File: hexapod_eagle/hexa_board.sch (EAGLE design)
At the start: 53 parts

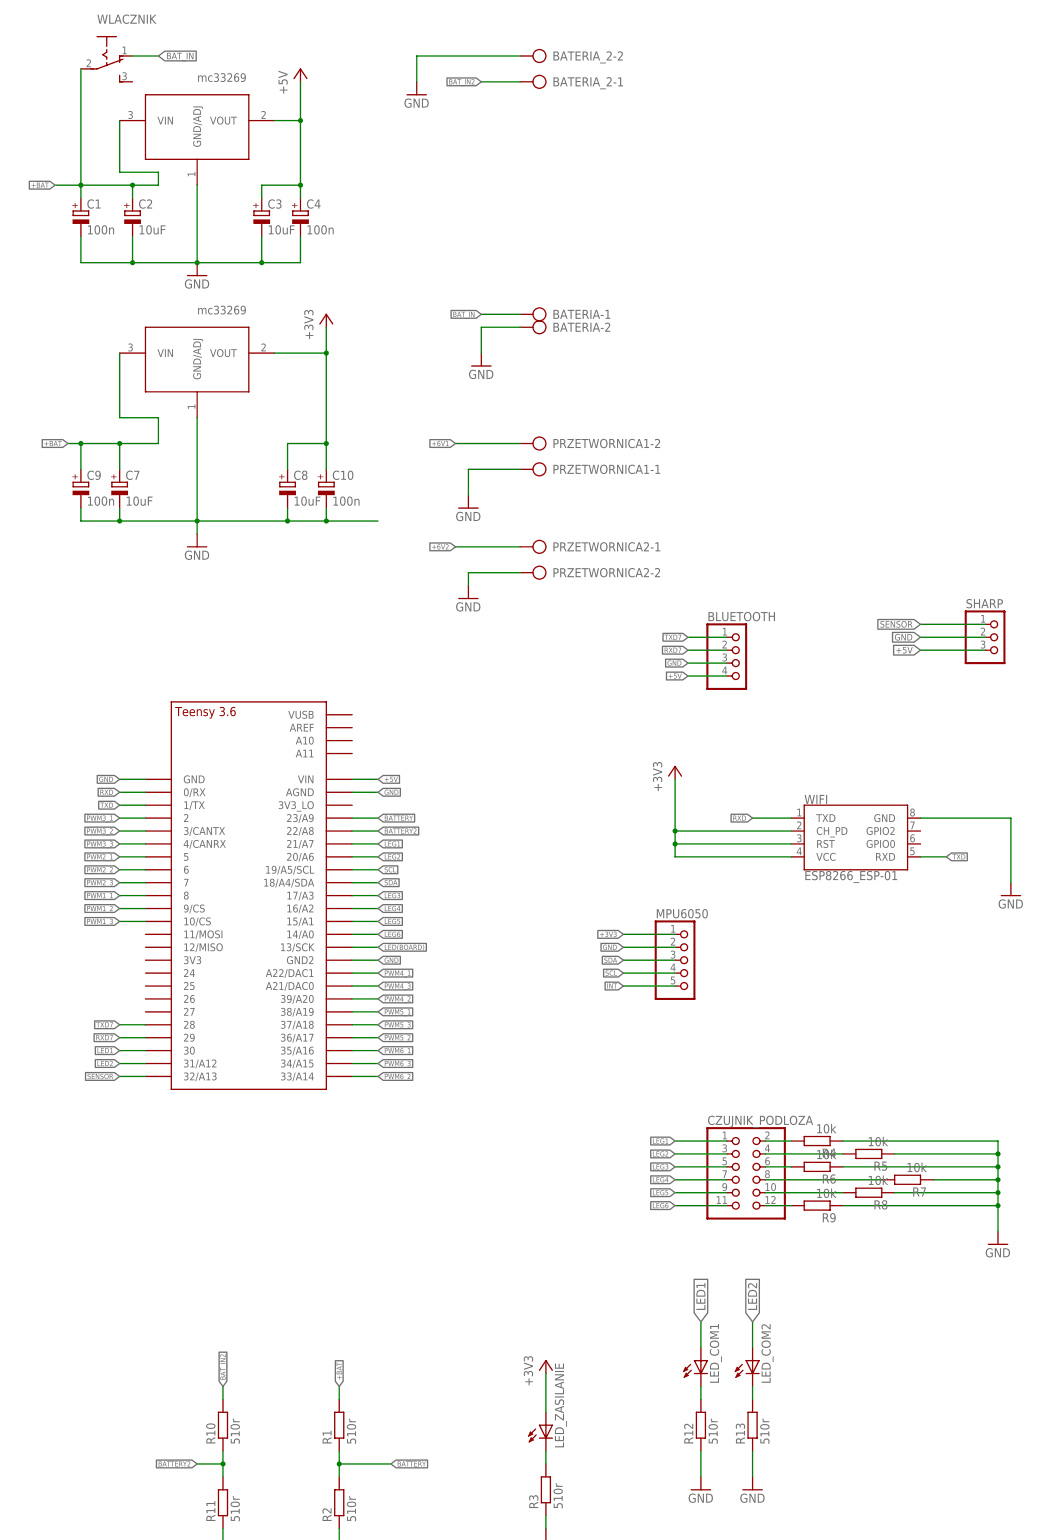
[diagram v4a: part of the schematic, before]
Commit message: Update eagle files
-change to ark leg sensor pins
-change isolte value
-esp32 cam-insted bluetooth/"wifi"
-some minor changes
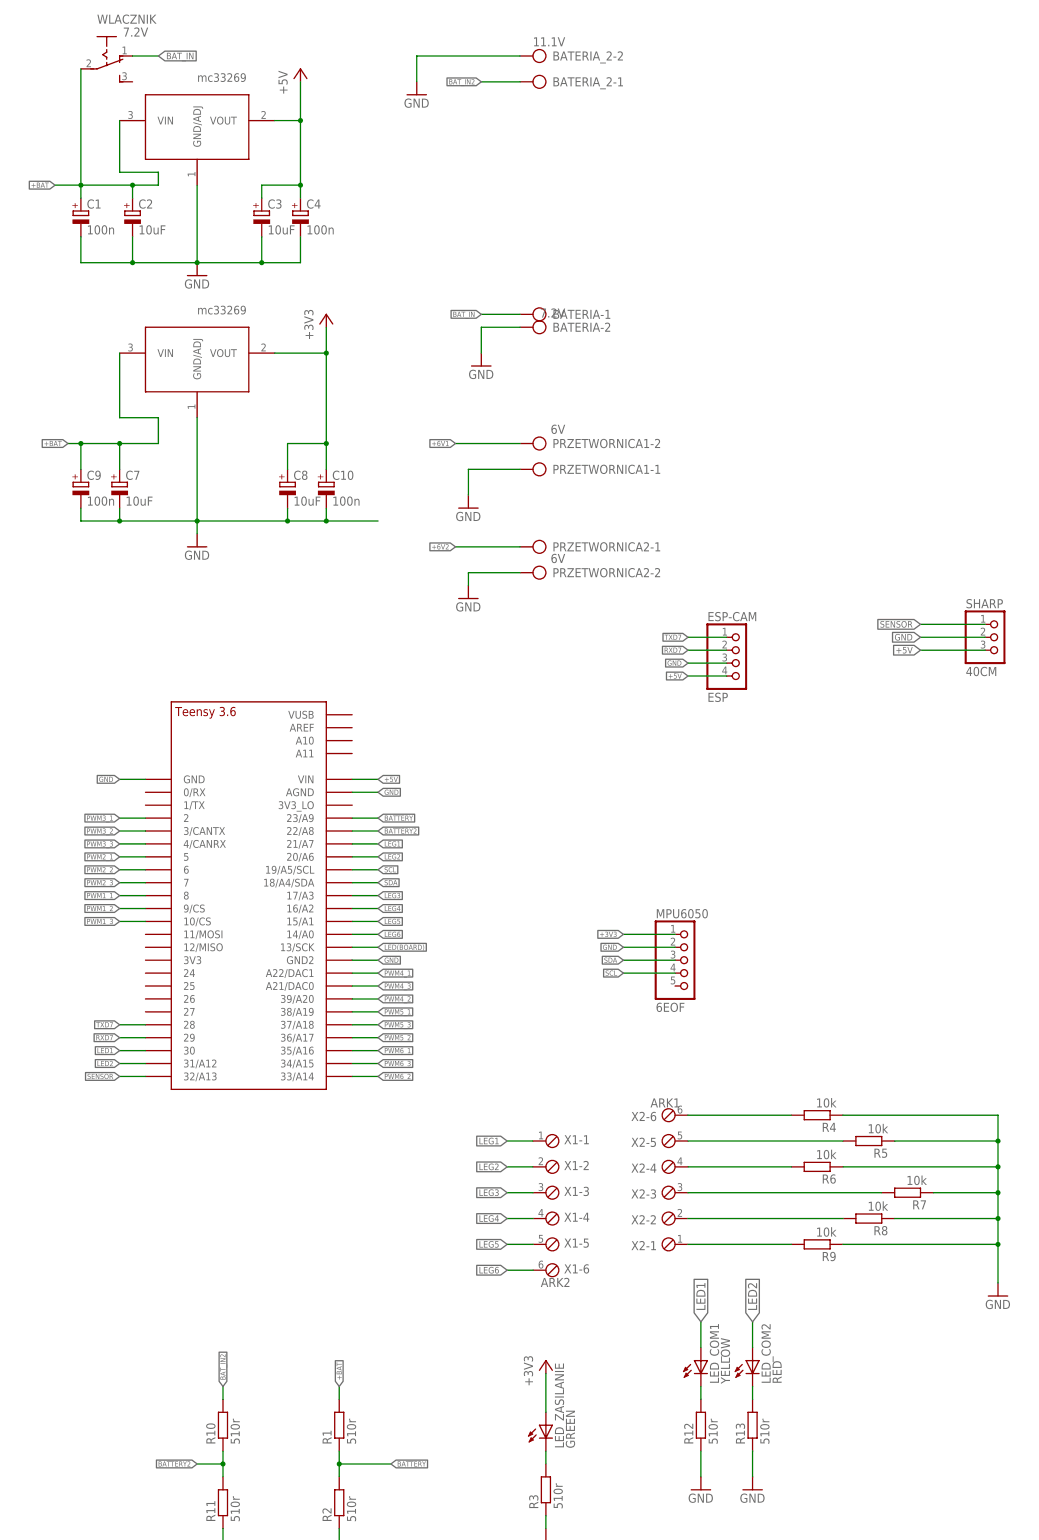
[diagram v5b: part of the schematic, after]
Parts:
- removed CZUJNIK_PODLOZA: (no value), pinhead:PINHD-2X6
- removed WIFI: ESP8266_ESP-01, SparkFun-RF:ESP8266_ESP-01
- added X1: ARK2, con-phoenix-254:MPT6
- added X2: ARK1, con-phoenix-254:MPT6
- BATERIA, WLACZNIK: value (none) -> 7.2V
- BATERIA_2: value (none) -> 11.1V
- ESP-CAM: value (none) -> ESP
- LED_COM1: value (none) -> YELLOW
- LED_COM2: value (none) -> RED
- LED_ZASILANIE: value (none) -> GREEN
- MPU6050: value (none) -> 6EOF
- PRZETWORNICA1, PRZETWORNICA2: value (none) -> 6V
- SHARP: value (none) -> 40CM
- renumbered BLUETOOTH to ESP-CAM
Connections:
- removed net INT: MPU6050.5
- removed net RXD: TEENSY41.0/RX, WIFI.TXD
- removed net TXD: TEENSY41.1/TX, WIFI.RXD
- net +3V3: no longer WIFI.CH_PD, WIFI.RST, WIFI.VCC
- net GND: no longer WIFI.GND
- net LEG1: now also X1-1.1; no longer CZUJNIK_PODLOZA.1
- net LEG2: now also X1-2.1; no longer CZUJNIK_PODLOZA.3
- net LEG3: now also X1-3.1; no longer CZUJNIK_PODLOZA.5
- net LEG4: now also X1-4.1; no longer CZUJNIK_PODLOZA.7
- net LEG5: now also X1-5.1; no longer CZUJNIK_PODLOZA.9
- net LEG6: now also X1-6.1; no longer CZUJNIK_PODLOZA.11
- net N$1: now also X2-6.1; no longer CZUJNIK_PODLOZA.2
- net N$2: now also X2-5.1; no longer CZUJNIK_PODLOZA.4
- net N$3: now also X2-4.1; no longer CZUJNIK_PODLOZA.6
- net N$5: now also X2-3.1; no longer CZUJNIK_PODLOZA.8
- net N$6: now also X2-2.1; no longer CZUJNIK_PODLOZA.10
- net N$7: now also X2-1.1; no longer CZUJNIK_PODLOZA.12
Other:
- moved on the sheet: R4, R5, R7, R8, R9

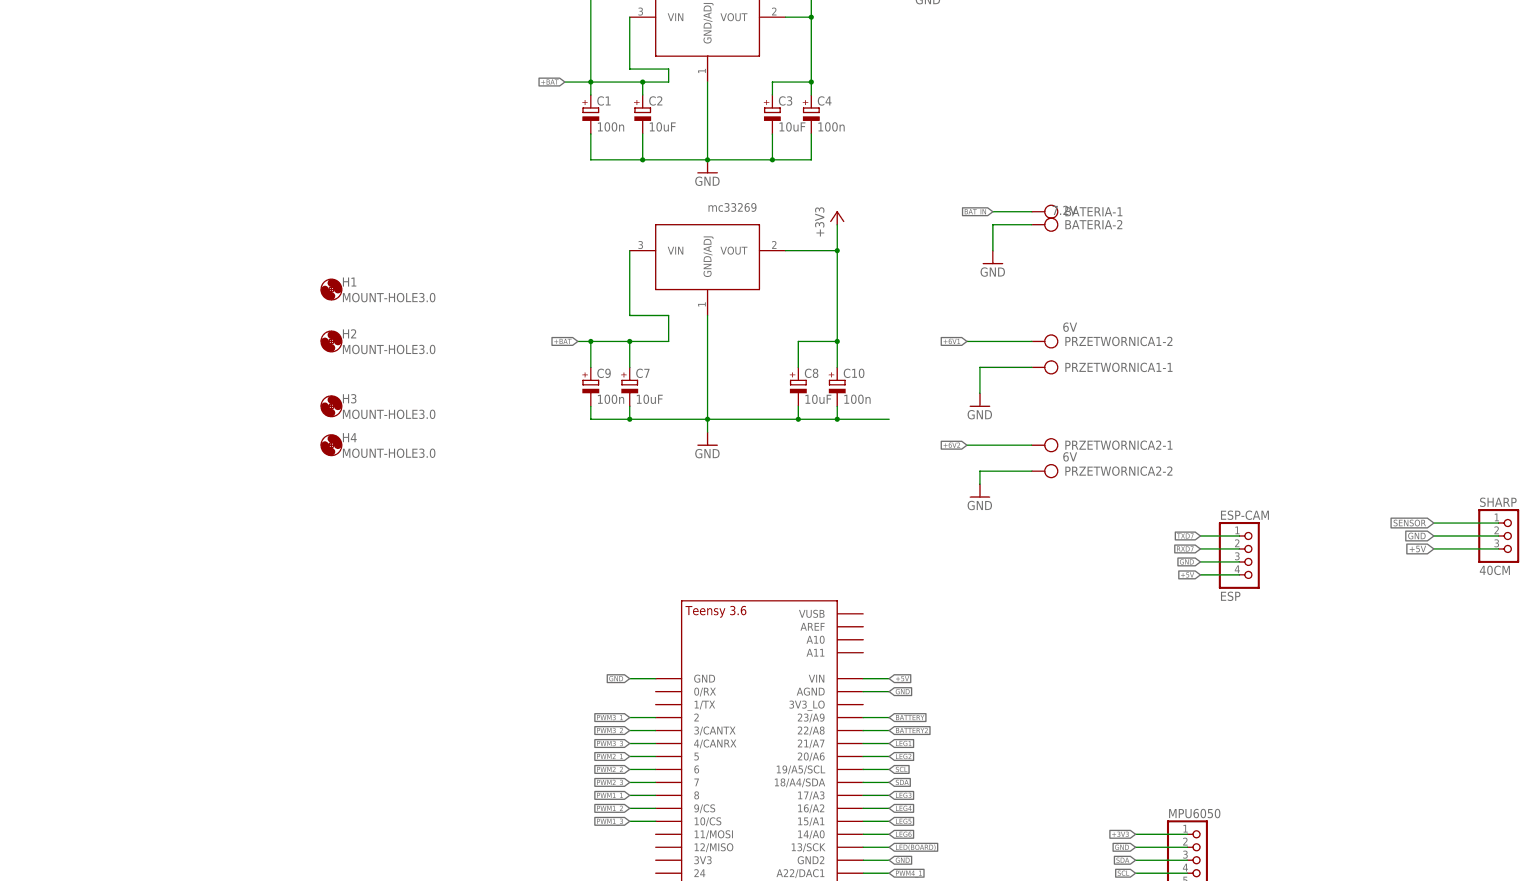
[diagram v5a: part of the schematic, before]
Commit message: Update eagle schematic and board
-added capacitors
-added voltage divider
-change package some capacitors
-added on/off swich for power mcu
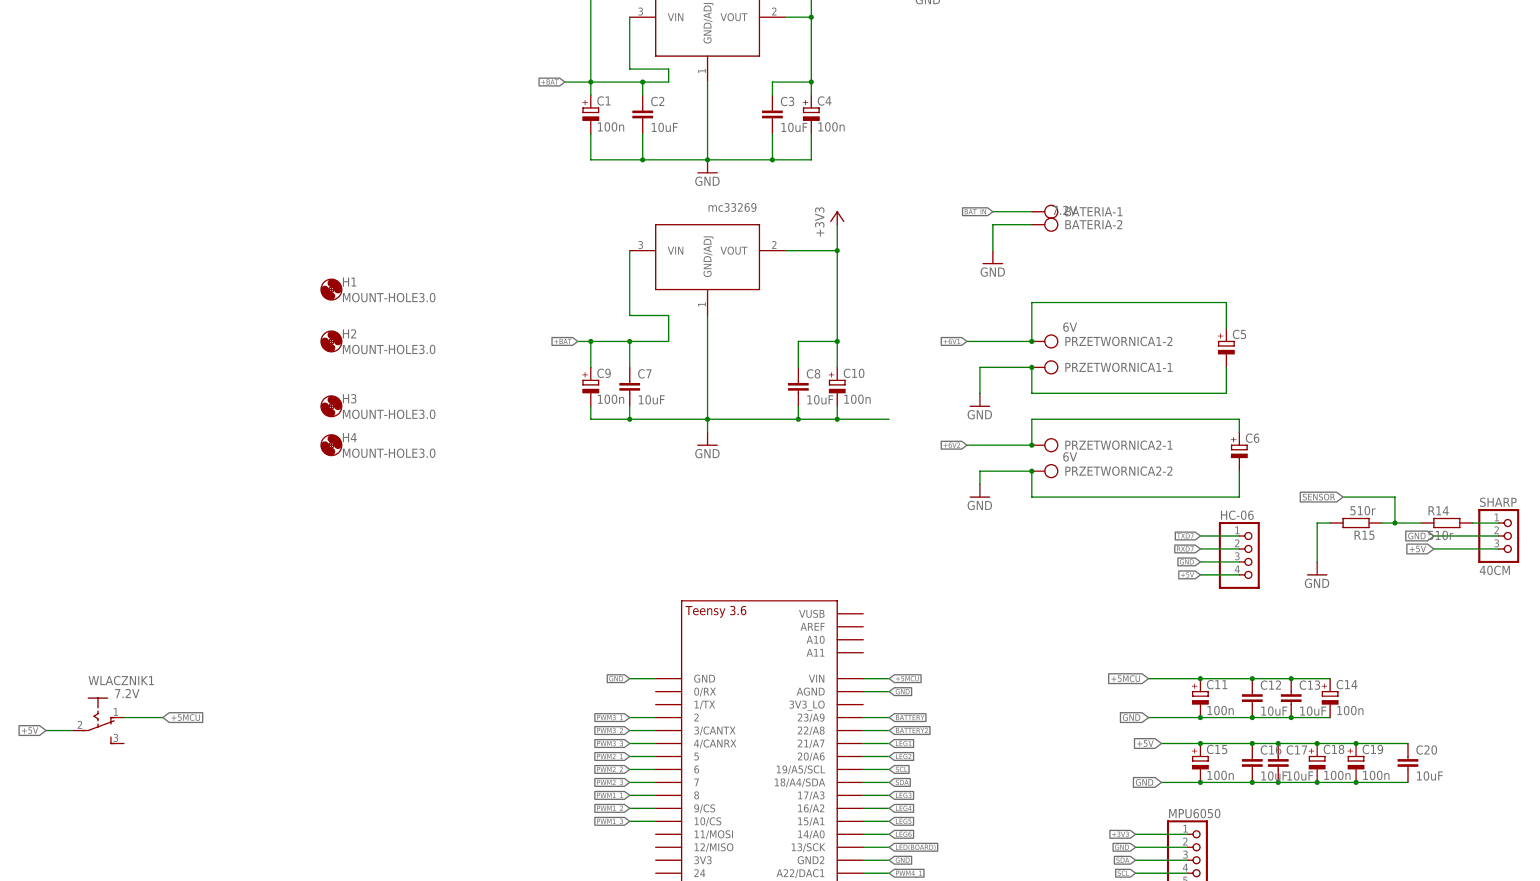
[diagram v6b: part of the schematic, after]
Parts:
- added C11, C14, C15, C18, C19: 100n, rcl:CPOL-EUSMCA
- added C12, C13, C16, C17, C20: 10uF, rcl:C-EUC1206
- added C5, C6: (no value), rcl:CPOL-EU150CLZ-1014
- added R14, R15: 510r, rcl:R-EU_R0805
- added WLACZNIK1: 7.2V, switch:255SB
- C2, C3, C7, C8: device rcl:CPOL-EUSMCB -> rcl:C-EUC1206
- HC-06: value ESP -> (none)
- renumbered ESP-CAM to HC-06
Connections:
- new net +5MCU: C11.+, C12.1, C13.1, C14.+, TEENSY41.VIN, WLACZNIK1.O
- new net N$10: R14.2, SHARP.1
- net +3V3: now also C8.1; no longer C8.+
- net +5V: now also C15.+, C16.1, C17.1, C18.+, C19.+, C20.1, C3.1, WLACZNIK1.P; no longer C3.+, TEENSY41.VIN
- net +6V1: now also C5.+
- net +6V2: now also C6.+
- net +BAT: now also C2.1, C7.1; no longer C2.+, C7.+
- net GND: now also C11.-, C12.2, C13.2, C14.-, C15.-, C16.2, C17.2, C18.-, C19.-, C2.2, C20.2, C3.2, C5.-, C6.-, C7.2, C8.2, R15.2; no longer C2.-, C3.-, C7.-, C8.-
- net SENSOR: now also R14.1, R15.1; no longer SHARP.1

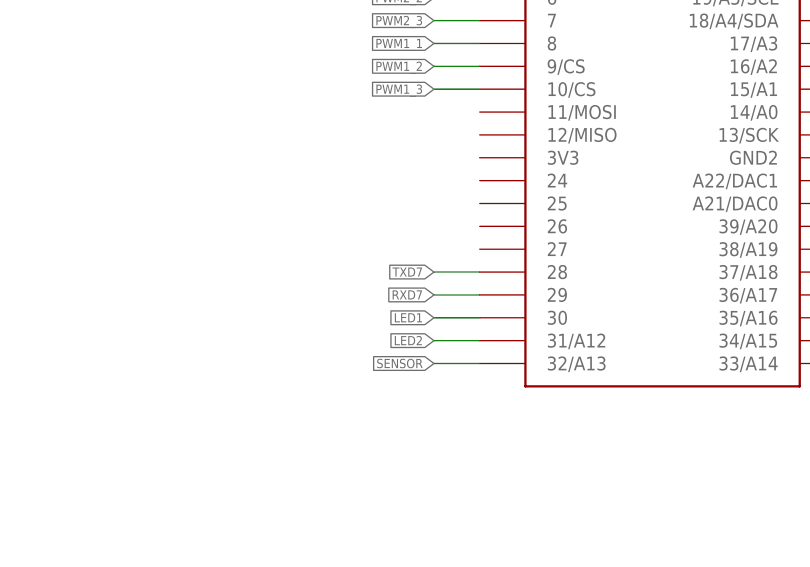
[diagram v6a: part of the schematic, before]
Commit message: Update eagle files
-change positions some capacitors
-change TXD/RXD lines
-minor changes
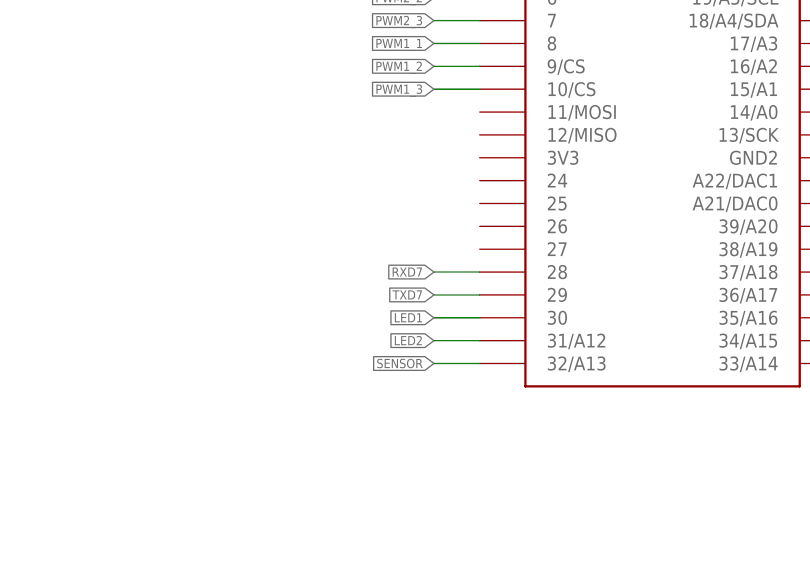
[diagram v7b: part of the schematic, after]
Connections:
- net RXD7: now also TEENSY41.28; no longer TEENSY41.29
- net TXD7: now also TEENSY41.29; no longer TEENSY41.28
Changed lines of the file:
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@@
 <net name="TXD7" class="0">
+<segment>
+<pinref part="HC-06" gate="A" pin="1"/>
+<wire x1="129.54" y1="180.34" x2="121.92" y2="180.34" width="0.1524" layer="91"/>
+<label x="121.92" y="180.34" size="1.016" layer="95" rot="R180" xref="yes"/>
+</segment>
+<segment>
+<pinref part="TEENSY41" gate="G$1" pin="29"/>
+<wire x1="15.24" y1="101.6" x2="10.16" y2="101.6" width="0.1524" layer="91"/>
+<label x="10.16" y="101.6" size="1.016" layer="95" rot="R180" xref="yes"/>
+</segment>
+</net>
+<net name="RXD7" class="0">
+<segment>
+<pinref part="HC-06" gate="A" pin="2"/>
+<wire x1="129.54" y1="177.8" x2="121.92" y2="177.8" width="0.1524" layer="91"/>
+<label x="121.92" y="177.8" size="1.016" layer="95" rot="R180" xref="yes"/>
+</segment>
 <segment>
 <pinref part="TEENSY41" gate="G$1" pin="28"/>
@@
 <label x="10.16" y="104.14" size="1.016" layer="95" rot="R180" xref="yes"/>
 </segment>
-<segment>
-<pinref part="HC-06" gate="A" pin="1"/>
-<wire x1="129.54" y1="180.34" x2="121.92" y2="180.34" width="0.1524" layer="91"/>
-<label x="121.92" y="180.34" size="1.016" layer="95" rot="R180" xref="yes"/>
-</segment>
 </net>
-<net name="RXD7" class="0">
-<segment>
-<pinref part="TEENSY41" gate="G$1" pin="29"/>
-<wire x1="15.24" y1="101.6" x2="10.16" y2="101.6" width="0.1524" layer="91"/>
-<label x="10.16" y="101.6" size="1.016" layer="95" rot="R180" xref="yes"/>
-</segment>
-<segment>
-<pinref part="HC-06" gate="A" pin="2"/>
-<wire x1="129.54" y1="177.8" x2="121.92" y2="177.8" width="0.1524" layer="91"/>
-<label x="121.92" y="177.8" size="1.016" layer="95" rot="R180" xref="yes"/>
-</segment>
-</net>
